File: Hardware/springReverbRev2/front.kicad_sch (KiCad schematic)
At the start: 51 parts, among them J915 DIP-8, J916 DIP-8, SW901 SW_SPDT_MSM, U1 TL072, U2 TL072

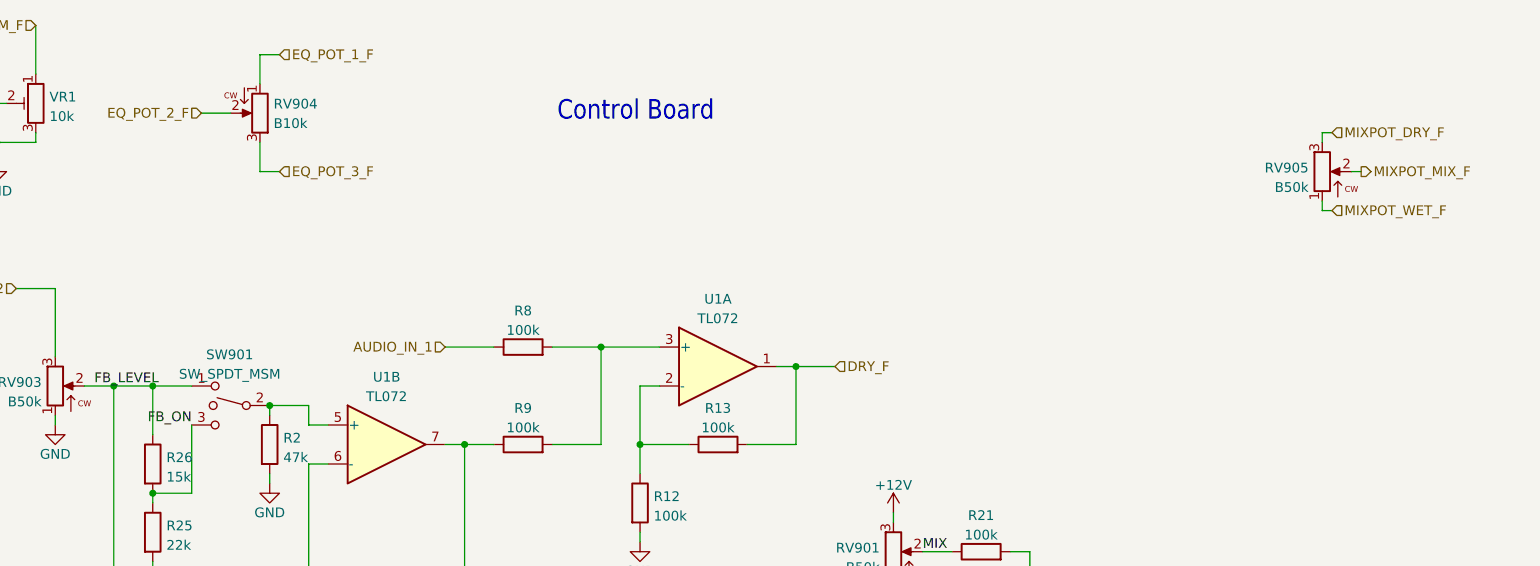
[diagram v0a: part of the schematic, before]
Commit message: Docs; make LED position consistent
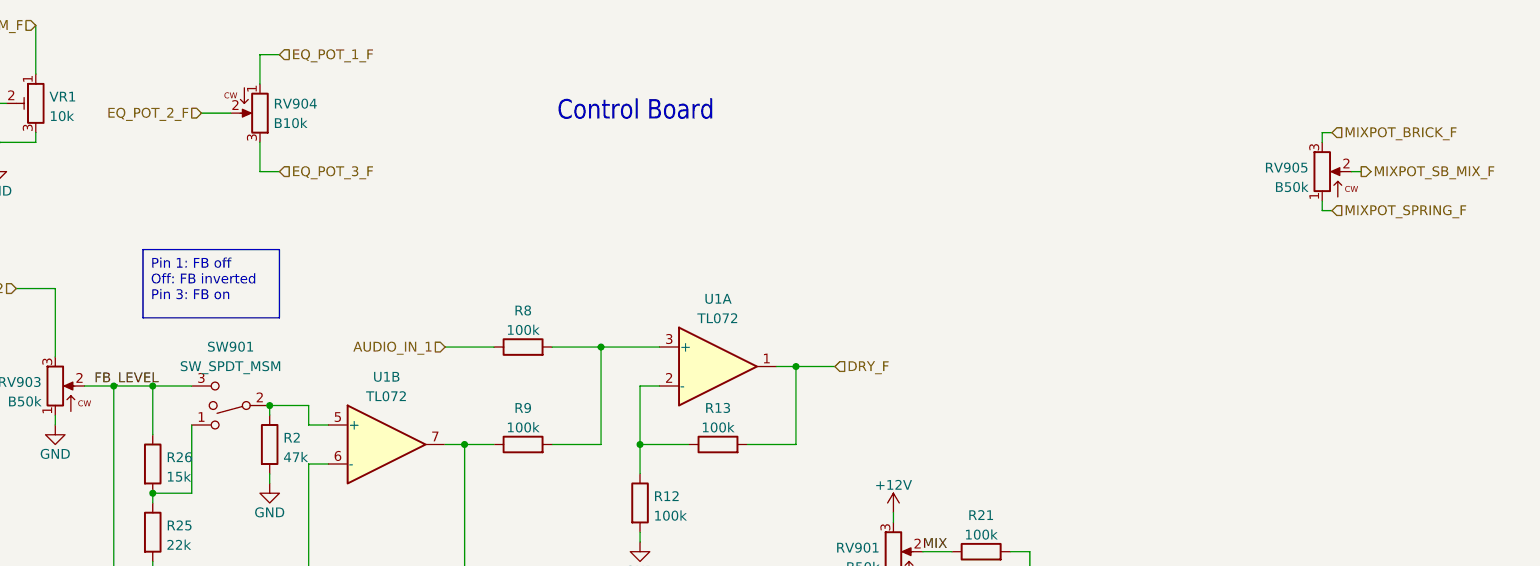
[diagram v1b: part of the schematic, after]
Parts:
- VR1: Manufacturer (none) -> Bourns; Part (none) -> 3362P
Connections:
- net FB_LEVEL: now also SW901.3; no longer SW901.1
- net FB_ON: no longer names the net of R25.1, R26.2
- net FB_ON: now also SW901.1; no longer SW901.3
- net MIXPOT_DRY_F renamed MIXPOT_BRICK_F
- net MIXPOT_MIX_F renamed MIXPOT_SB_MIX_F
- net MIXPOT_WET_F renamed MIXPOT_SPRING_F
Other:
- moved on the sheet: SW901
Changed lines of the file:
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@@
     (fill (type none))
+  )
+  (text_box "Pin 1: FB off\nOff: FB inverted\nPin 3: FB on"
+    (at 64.77 52.07 0) (size 17.78 8.89)
+    (stroke (width 0) (type default))
+    (fill (type none))
+    (effects (font (size 1.27 1.27)) (justify left top))
   )
   (text "HARDWARE" (at 177.8 147.32 0)
@@
     (effects (font (size 1.27 1.27)) (justify left bottom))
   )
-  (label "FB_ON" (at 71.12 74.93 180) (fields_autoplaced)
-    (effects (font (size 1.27 1.27)) (justify right bottom))
-  )
   (hierarchical_label "CV_IN" (shape input) (at 125.73 106.68 180) (fields_autoplaced)
     (effects (font (size 1.27 1.27)) (justify right))
@@
     (effects (font (size 1.27 1.27)) (justify right))
   )
-  (hierarchical_label "MIXPOT_MIX_F" (shape output) (at 223.52 41.91 0) (fields_autoplaced)
+  (hierarchical_label "MIXPOT_SB_MIX_F" (shape output) (at 223.52 41.91 0) (fields_autoplaced)
     (effects (font (size 1.27 1.27)) (justify left))
   )
@@
     (effects (font (size 1.27 1.27)) (justify left))
   )
-  (hierarchical_label "MIXPOT_DRY_F" (shape input) (at 219.71 36.83 0) (fields_autoplaced)
+  (hierarchical_label "MIXPOT_BRICK_F" (shape input) (at 219.71 36.83 0) (fields_autoplaced)
     (effects (font (size 1.27 1.27)) (justify left))
   )
@@
     (effects (font (size 1.27 1.27)) (justify left))
   )
-  (hierarchical_label "MIXPOT_WET_F" (shape input) (at 219.71 46.99 0) (fields_autoplaced)
+  (hierarchical_label "MIXPOT_SPRING_F" (shape input) (at 219.71 46.99 0) (fields_autoplaced)
     (effects (font (size 1.27 1.27)) (justify left))
   )
@@
       (effects (font (size 1.27 1.27)) hide)
     )
+    (property "Description" "16 mm potentiometer" (at 53.34 69.85 0)
+      (effects (font (size 1.27 1.27)) hide)
+    )
     (pin "1")
     (pin "2")
@@
       (effects (font (size 1.27 1.27)) hide)
     )
+    (property "Description" "16 mm potentiometer" (at 139.7 114.3 0)
+      (effects (font (size 1.27 1.27)) hide)
+    )
     (pin "1")
     (pin "2")
@@
       (effects (font (size 1.27 1.27)) hide)
     )
-    (property "Manufacturer" "" (at 50.8 33.02 0)
-      (effects (font (size 1.27 1.27)) hide)
-    )
-    (property "Part" "" (at 50.8 33.02 0)
+    (property "Manufacturer" "Bourns" (at 50.8 33.02 0)
+      (effects (font (size 1.27 1.27)) hide)
+    )
+    (property "Part" "3362P" (at 50.8 33.02 0)
+      (effects (font (size 1.27 1.27)) hide)
+    )
+    (property "Description" "Trim potentiometer" (at 50.8 33.02 0)
       (effects (font (size 1.27 1.27)) hide)
     )
@@
       (effects (font (size 1.27 1.27)) hide)
     )
-    (property "Description" "Ceramic capacitor" (at 50.8 139.7 0)
+    (property "Description" "Ceramic capacitor, 2.5 mm pitch" (at 50.8 139.7 0)
       (effects (font (size 1.27 1.27)) hide)
     )
@@
       (effects (font (size 1.27 1.27)) hide)
     )
-    (property "Description" "Ceramic capacitor" (at 78.74 147.32 0)
+    (property "Description" "Ceramic capacitor, 2.5 mm pitch" (at 78.74 147.32 0)
       (effects (font (size 1.27 1.27)) hide)
     )
@@
       (effects (font (size 1.27 1.27)) hide)
     )
-    (property "Description" "Ceramic capacitor" (at 50.8 147.32 0)
+    (property "Description" "Ceramic capacitor, 2.5 mm pitch" (at 50.8 147.32 0)
       (effects (font (size 1.27 1.27)) hide)
     )
@@
     )
     (property "Part" "" (at 162.56 91.44 0)
+      (effects (font (size 1.27 1.27)) hide)
+    )
+    (property "Description" "16 mm potentiometer" (at 162.56 91.44 0)
       (effects (font (size 1.27 1.27)) hide)
     )
@@
     )
     (property "Part" "" (at 218.44 41.91 0)
+      (effects (font (size 1.27 1.27)) hide)
+    )
+    (property "Description" "16 mm potentiometer" (at 218.44 41.91 0)
       (effects (font (size 1.27 1.27)) hide)
     )
@@
       (effects (font (size 1.27 1.27)) hide)
     )
+    (property "Description" "16 mm potentiometer" (at 80.01 34.29 0)
+      (effects (font (size 1.27 1.27)) hide)
+    )
     (pin "1")
     (pin "2")
@@
       (effects (font (size 1.27 1.27)) hide)
     )
-    (property "Description" "Ceramic capacitor" (at 78.74 139.7 0)
+    (property "Description" "Ceramic capacitor, 2.5 mm pitch" (at 78.74 139.7 0)
       (effects (font (size 1.27 1.27)) hide)
     )
@@
     )
   )
-  (symbol (lib_id "AO_symbols:SW_SPDT_MSM") (at 76.2 72.39 0) (mirror y) (unit 1)
-    (in_bom yes) (on_board yes) (dnp no) (fields_autoplaced)
-    (property "Reference" "SW901" (at 76.073 65.7692 0)
-      (effects (font (size 1.27 1.27)))
-    )
-    (property "Value" "SW_SPDT_MSM" (at 76.073 68.3061 0)
-      (effects (font (size 1.27 1.27)))
-    )
+  (symbol (lib_id "AO_symbols:SW_SPDT_MSM") (at 76.2 72.39 180) (unit 1)
+    (in_bom yes) (on_board yes) (dnp no)
+    (property "Reference" "SW901" (at 76.2 64.77 0)
+      (effects (font (size 1.27 1.27)))
+    )
+    (property "Value" "SW_SPDT_MSM" (at 76.2 67.31 0)
+      (effects (font (size 1.27 1.27)))
+    )
